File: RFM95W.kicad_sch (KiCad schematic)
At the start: 1 part, among them U2 RFM95W-915S2

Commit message: some cleanup. About to split two lra module branches.
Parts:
- U2: now fitted
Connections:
- net DI0 renamed DIO0
- net DI1 renamed DIO1
- net DI2: no longer names the net of U2.16 (DIO2)
- net DI3: no longer names the net of U2.11 (DIO3)
- net DI4: no longer names the net of U2.12 (DIO4)
- net DI5: no longer names the net of U2.7 (DIO5)
- no-connect marks 1 -> 5

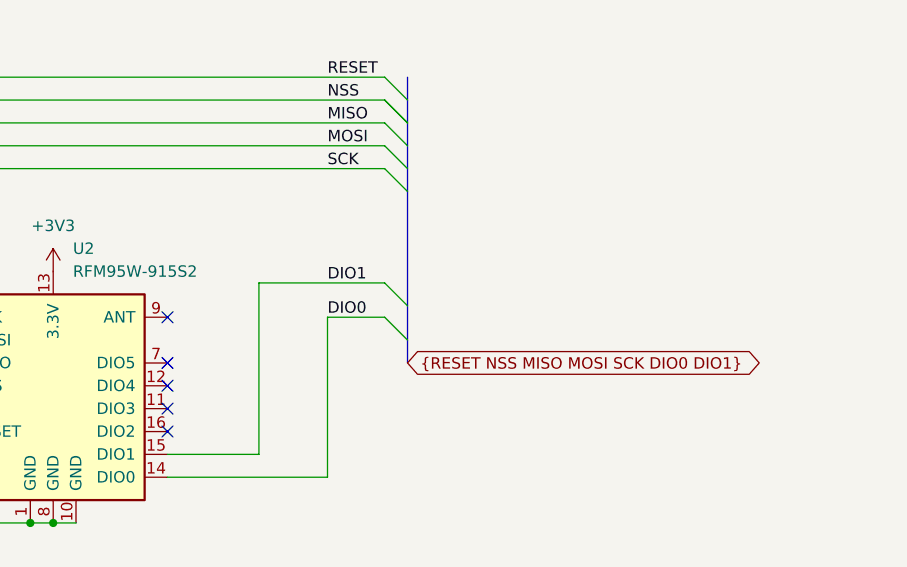
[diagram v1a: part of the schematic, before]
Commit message: added antenna connector.
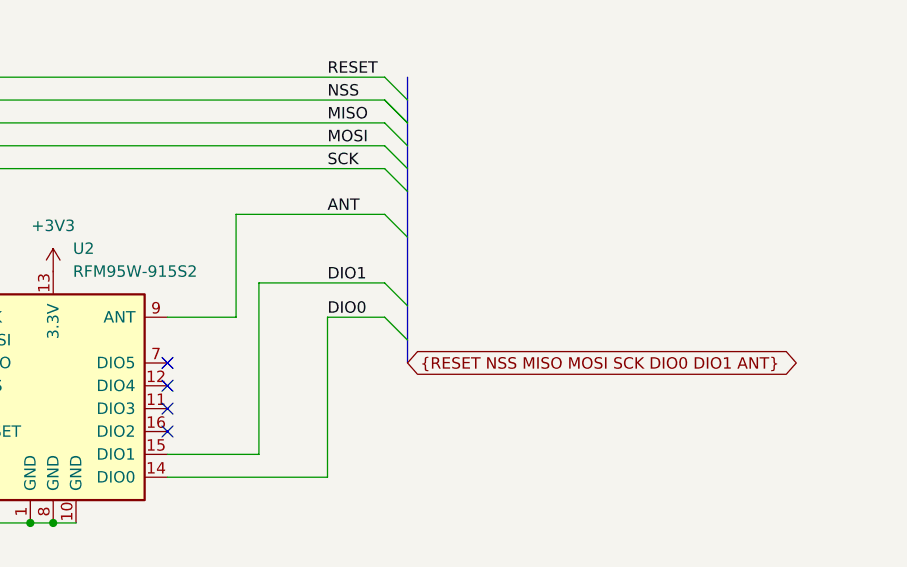
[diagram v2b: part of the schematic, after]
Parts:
- U2: Manufacturer (none) -> HopeRF; MfgPart (none) -> RFM95W-915S2; MountType (none) -> SMT; Notes (none) -> or equivalent
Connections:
- net ANT: now reaches U2.9 (ANT)
- no-connect marks 5 -> 4
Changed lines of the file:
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@@
-	)
-	(no_connect
-		(at 128.27 77.47)
 	)
 	(no_connect
@@
 	)
 	(bus_entry
+		(at 154.94 68.58)
+		(size -2.54 -2.54)
+		(stroke
+			(width 0)
+			(type default)
+		)
+	)
+	(bus_entry
 		(at 154.94 80.01)
 		(size -2.54 -2.54)
@@
 	(wire
 		(pts
+			(xy 135.89 66.04) (xy 135.89 77.47)
+		)
+		(stroke
+			(width 0)
+			(type default)
+		)
+	)
+	(wire
+		(pts
 			(xy 100.33 82.55) (xy 100.33 55.88)
 		)
@@
 		)
 	)
+	(bus
+		(pts
+			(xy 154.94 68.58) (xy 154.94 76.2)
+		)
+		(stroke
+			(width 0)
+			(type default)
+		)
+	)
 	(wire
 		(pts
@@
 	(wire
 		(pts
+			(xy 135.89 77.47) (xy 128.27 77.47)
+		)
+		(stroke
+			(width 0)
+			(type default)
+		)
+	)
+	(wire
+		(pts
 			(xy 100.33 55.88) (xy 152.4 55.88)
 		)
@@
 		)
 	)
-	(bus
-		(pts
-			(xy 154.94 63.5) (xy 154.94 76.2)
+	(wire
+		(pts
+			(xy 135.89 66.04) (xy 152.4 66.04)
+		)
+		(stroke
+			(width 0)
+			(type default)
+		)
+	)
+	(bus
+		(pts
+			(xy 154.94 63.5) (xy 154.94 68.58)
 		)
 		(stroke
@@
 		)
 	)
+	(label "ANT"
+		(at 146.05 66.04 0)
+		(effects
+			(font
+				(size 1.27 1.27)
+			)
+			(justify left bottom)
+		)
+	)
 	(label "SCK"
 		(at 146.05 60.96 0)
@@
 		)
 	)
-	(global_label "{RESET NSS MISO MOSI SCK DIO0 DIO1}"
+	(global_label "{RESET NSS MISO MOSI SCK DIO0 DIO1 ANT}"
 		(shape bidirectional)
 		(at 154.94 82.55 0)
@@
 		)
 		(property "Intersheetrefs" "${INTERSHEET_REFS}"
-			(at 197.8016 82.55 0)
+			(at 202.1559 82.55 0)
 			(effects
 				(font
@@
 			)
 		)
-		(property "Datasheet" "https://www.hoperf.com/data/upload/portal/20181127/5bfcbea20e9ef.pdf"
+		(property "Datasheet" "https://www.hoperf.com/modules/lora/RFM95W.html"
 			(at 31.75 43.18 0)
 			(effects
@@
 			)
 		)
-		(property "Description" "Low power long range transceiver module, SPI and parallel interface, 868 MHz, spreading factor 6 to12, bandwidth 7.8 to 500kHz, -111 to -148 dBm, SMD-16, DIP-16"
+		(property "Description" "LoRa module, SPI, 915MHz, spreading factor 6 to12, bandwidth 125 to 500kHz, -111 to -136 dBm, SMD-16"
 			(at 115.57 85.09 0)
 			(effects
+				(font
+					(size 1.27 1.27)
+				)
+				(hide yes)
+			)
+		)
+		(property "MountType" "SMT"
+			(at 115.57 85.09 0)
+			(effects
+				(font
+					(size 1.27 1.27)
+				)
+				(hide yes)
+			)
+		)
+		(property "Notes" "or equivalent"
+			(at 115.57 85.09 0)
+			(effects
+				(font
+					(size 1.27 1.27)
+				)
+				(hide yes)
+			)
+		)
+		(property "Manufacturer" "HopeRF"
+			(at 115.57 85.09 0)
+			(effects
+				(font
+					(size 1.27 1.27)
+				)
+				(hide yes)
+			)
+		)
+		(property "MfgPart" "RFM95W-915S2"
+			(at 115.57 85.09 0)
+			(effects

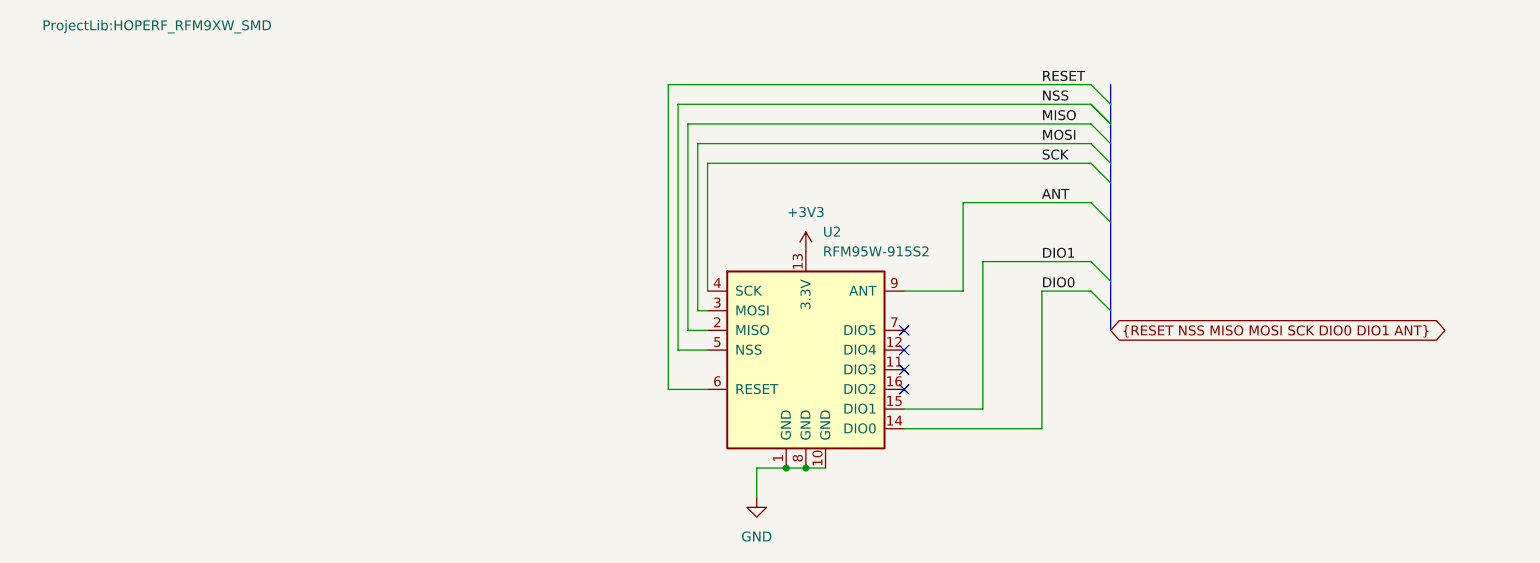
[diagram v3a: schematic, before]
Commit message: added 10k pullup on NSS.
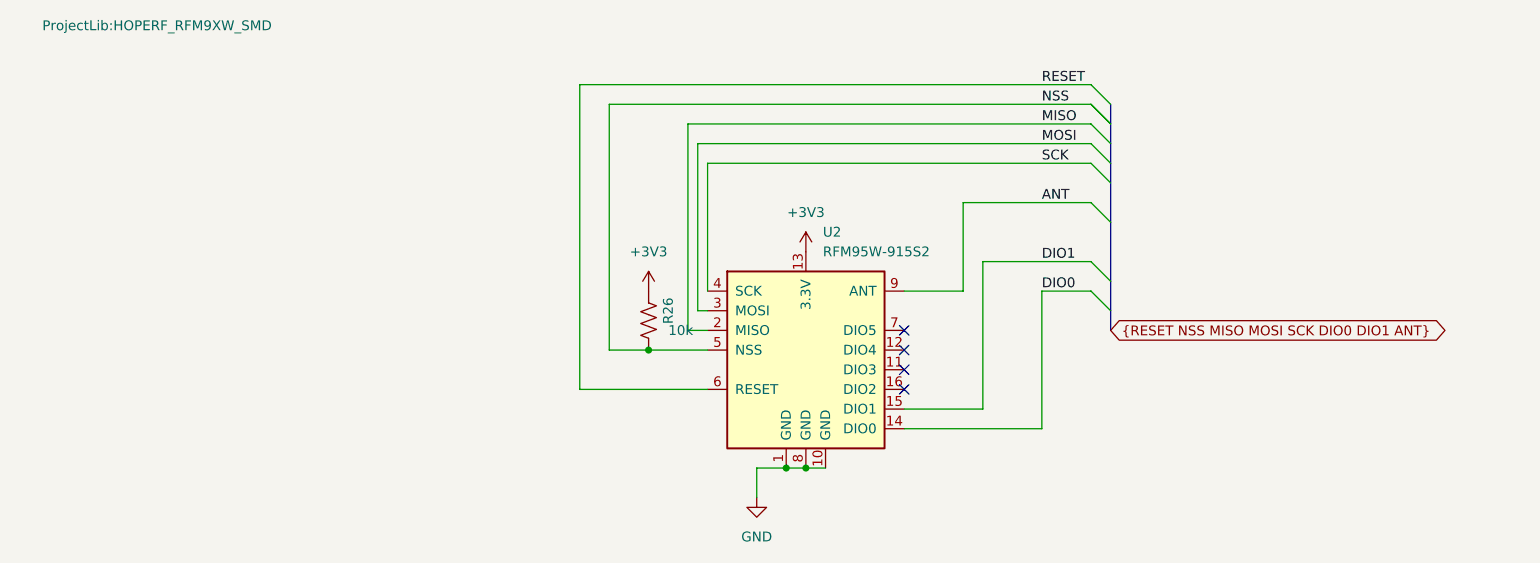
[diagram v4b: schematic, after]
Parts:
- added R26: 10k, ProjectLib:R_0603_1608Metric, symbol ProjectLib:R_US
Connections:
- net +3V3: now also R26.1
- net NSS: now also R26.2
